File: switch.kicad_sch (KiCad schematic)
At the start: 46 parts, among them Q1 2N7002, U1 RTL8367RB, Y1 25MHz

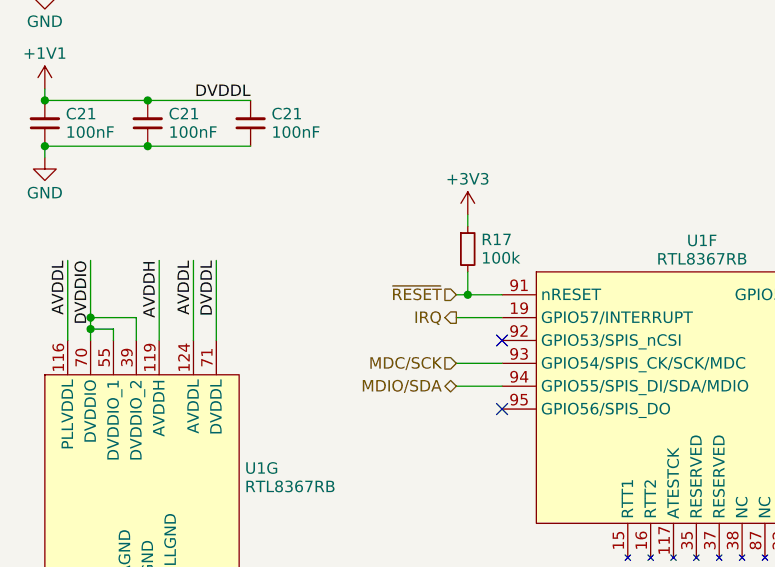
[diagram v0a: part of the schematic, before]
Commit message: Finalize design
- Layout last signals
- Hide designators
- Add more LEDs
- Add tooling holes
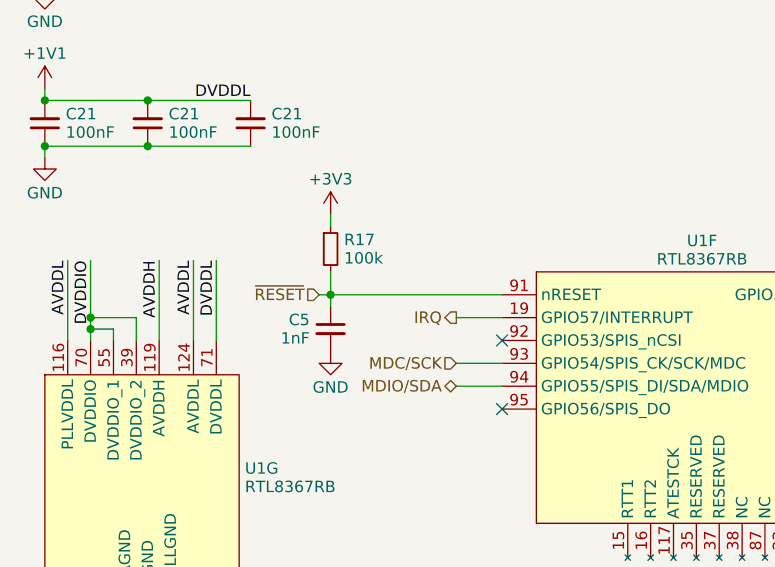
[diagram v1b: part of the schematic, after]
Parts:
- added C5: 1nF, Capacitor_SMD:C_0402_1005Metric, symbol Device:C_Small
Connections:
- net GND: now also C5.2
- net ~{RESET}: now also C5.1
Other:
- moved on the sheet: R17
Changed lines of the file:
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@@
   (junction (at 39.37 77.47) (diameter 0) (color 0 0 0 0)
   )
-  (junction (at 63.5 138.43) (diameter 0) (color 0 0 0 0)
+  (junction (at 48.26 138.43) (diameter 0) (color 0 0 0 0)
   )
   (junction (at 21.59 140.97) (diameter 0) (color 0 0 0 0)
@@
     (stroke (width 0) (type default))
   )
-  (wire (pts (xy 63.5 138.43) (xy 67.31 138.43))
+  (wire (pts (xy 48.26 138.43) (xy 67.31 138.43))
     (stroke (width 0) (type default))
   )
@@
     (stroke (width 0) (type default))
   )
-  (wire (pts (xy 63.5 129.54) (xy 63.5 130.81))
+  (wire (pts (xy 48.26 129.54) (xy 48.26 130.81))
     (stroke (width 0) (type default))
   )
@@
     (stroke (width 0) (type default))
   )
-  (wire (pts (xy 62.23 138.43) (xy 63.5 138.43))
+  (wire (pts (xy 46.99 138.43) (xy 48.26 138.43))
+    (stroke (width 0) (type default))
+  )
+  (wire (pts (xy 48.26 138.43) (xy 48.26 139.7))
     (stroke (width 0) (type default))
   )
@@
     (stroke (width 0) (type default))
   )
-  (wire (pts (xy 63.5 135.89) (xy 63.5 138.43))
+  (wire (pts (xy 48.26 135.89) (xy 48.26 138.43))
     (stroke (width 0) (type default))
   )
@@
     (effects (font (size 1.27 1.27)) (justify left))
   )
-  (hierarchical_label "~{RESET}" (shape input) (at 62.23 138.43 180) (fields_autoplaced)
+  (hierarchical_label "~{RESET}" (shape input) (at 46.99 138.43 180) (fields_autoplaced)
     (effects (font (size 1.27 1.27)) (justify right))
   )
@@
     )
   )
-  (symbol (lib_id "Device:R_Small") (at 63.5 133.35 0) (unit 1)
-    (in_bom yes) (on_board yes) (dnp no) (fields_autoplaced)
-    (property "Reference" "R17" (at 64.9986 132.326 0)
+  (symbol (lib_id "Device:R_Small") (at 48.26 133.35 0) (unit 1)
+    (in_bom yes) (on_board yes) (dnp no) (fields_autoplaced)
+    (property "Reference" "R17" (at 49.7586 132.326 0)
       (effects (font (size 1.27 1.27)) (justify left))
     )
-    (property "Value" "100k" (at 64.9986 134.374 0)
+    (property "Value" "100k" (at 49.7586 134.374 0)
       (effects (font (size 1.27 1.27)) (justify left))
     )
-    (property "Footprint" "Resistor_SMD:R_0402_1005Metric" (at 63.5 133.35 0)
-      (effects (font (size 1.27 1.27)) hide)
-    )
-    (property "Datasheet" "~" (at 63.5 133.35 0)
-      (effects (font (size 1.27 1.27)) hide)
-    )
-    (property "LCSC" "C25741" (at 63.5 133.35 0)
+    (property "Footprint" "Resistor_SMD:R_0402_1005Metric" (at 48.26 133.35 0)
+      (effects (font (size 1.27 1.27)) hide)
+    )
+    (property "Datasheet" "~" (at 48.26 133.35 0)
+      (effects (font (size 1.27 1.27)) hide)
+    )
+    (property "LCSC" "C25741" (at 48.26 133.35 0)
       (effects (font (size 1.27 1.27)) hide)
     )
@@
         (path "/1d58c53f-167c-46c6-b61a-0c5d76c66e31/71e1ec36-fcc5-4ea9-a9bb-92fd21a85ab0"
           (reference "R79") (unit 1)
+        )
+      )
+    )
+  )
+  (symbol (lib_id "Device:C_Small") (at 48.26 142.24 0) (mirror y) (unit 1)
+    (in_bom yes) (on_board yes) (dnp no)
+    (property "Reference" "C5" (at 45.9359 141.2223 0)
+      (effects (font (size 1.27 1.27)) (justify left))
+    )
+    (property "Value" "1nF" (at 45.9359 143.2703 0)
+      (effects (font (size 1.27 1.27)) (justify left))
+    )
+    (property "Footprint" "Capacitor_SMD:C_0402_1005Metric" (at 48.26 142.24 0)
+      (effects (font (size 1.27 1.27)) hide)
+    )
+    (property "Datasheet" "~" (at 48.26 142.24 0)
+      (effects (font (size 1.27 1.27)) hide)
+    )
+    (property "LCSC" "C1523" (at 48.26 142.24 0)
+      (effects (font (size 1.27 1.27)) hide)
+    )
+    (pin "1")
+    (pin "2")
+    (instances
+      (project "OpenHomeSwitch"
+        (path "/1d58c53f-167c-46c6-b61a-0c5d76c66e31/71e1ec36-fcc5-4ea9-a9bb-92fd21a85ab0/fcbac710-5c4c-4f73-a659-520d2a4da378"
+          (reference "C5") (unit 1)
+        )
+        (path "/1d58c53f-167c-46c6-b61a-0c5d76c66e31/71e1ec36-fcc5-4ea9-a9bb-92fd21a85ab0"
+          (reference "C130") (unit 1)
         )
       )
@@
     )
   )
+  (symbol (lib_id "power:GND") (at 48.26 144.78 0) (unit 1)
+    (in_bom yes) (on_board yes) (dnp no) (fields_autoplaced)
+    (property "Reference" "#PWR0141" (at 48.26 151.13 0)
+      (effects (font (size 1.27 1.27)) hide)
+    )
+    (property "Value" "GND" (at 48.26 148.725 0)
+      (effects (font (size 1.27 1.27)))
+    )
+    (property "Footprint" "" (at 48.26 144.78 0)
+      (effects (font (size 1.27 1.27)) hide)
+    )
+    (property "Datasheet" "" (at 48.26 144.78 0)
+      (effects (font (size 1.27 1.27)) hide)
+    )
+    (pin "1")
+    (instances
+      (project "OpenHomeSwitch"
+        (path "/1d58c53f-167c-46c6-b61a-0c5d76c66e31/71e1ec36-fcc5-4ea9-a9bb-92fd21a85ab0"
+          (reference "#PWR0141") (unit 1)
+        )
+      )
+    )
+  )
   (symbol (lib_id "Device:C_Small") (at 201.93 113.03 90) (mirror x) (unit 1)
     (in_bom yes) (on_board yes) (dnp no)
@@
     )
   )
-  (symbol (lib_id "power:+3V3") (at 63.5 129.54 0) (unit 1)
-    (in_bom yes) (on_board yes) (dnp no) (fields_autoplaced)
-    (property "Reference" "#PWR0128" (at 63.5 133.35 0)
-      (effects (font (size 1.27 1.27)) hide)
-    )
-    (property "Value" "+3V3" (at 63.5 125.595 0)
-      (effects (font (size 1.27 1.27)))
-    )
-    (property "Footprint" "" (at 63.5 129.54 0)
-      (effects (font (size 1.27 1.27)) hide)
-    )
-    (property "Datasheet" "" (at 63.5 129.54 0)
-      (effects (font (size 1.27 1.27)) hide)
-    )
+  (symbol (lib_id "power:+3V3") (at 48.26 129.54 0) (unit 1)
+    (in_bom yes) (on_board yes) (dnp no) (fields_autoplaced)
+    (property "Reference" "#PWR0128" (at 48.26 133.35 0)
+      (effects (font (size 1.27 1.27)) hide)
+    )
+    (property "Value" "+3V3" (at 48.26 125.595 0)
+      (effects (font (size 1.27 1.27)))
+    )
+    (property "Footprint" "" (at 48.26 129.54 0)
+      (effects (font (size 1.27 1.27)) hide)
+    )
+    (property "Datasheet" "" (at 48.26 129.54 0)
+      (effects (font (size 1.27 1.27)) hide)
+    )

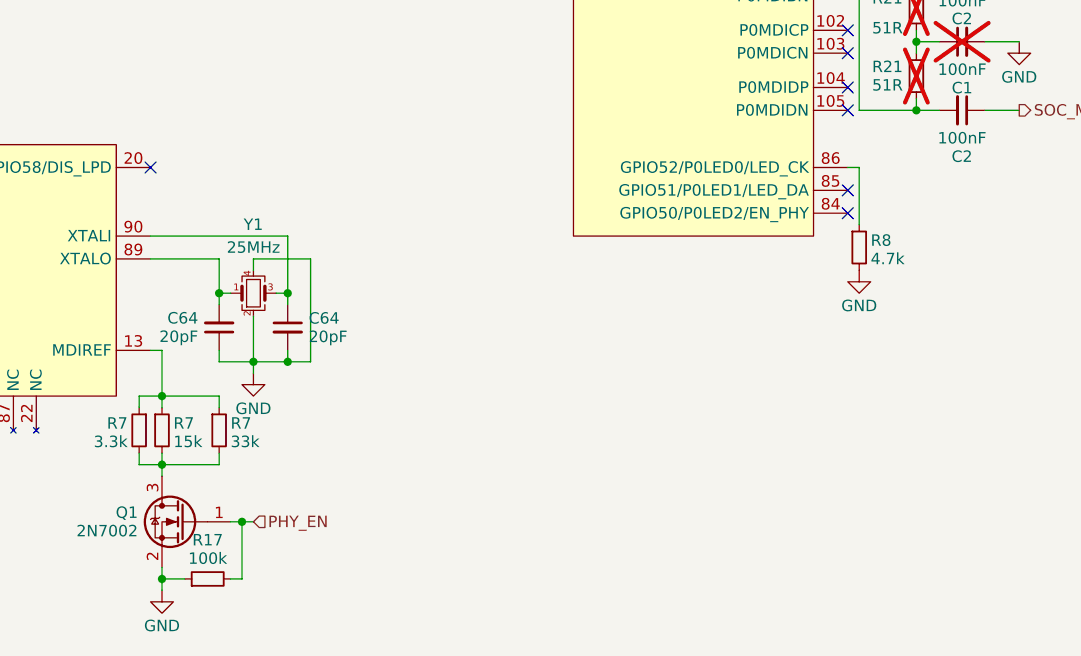
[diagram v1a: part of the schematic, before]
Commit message: Change switch control to I2C
MDIO has proven too slow, use I2C instead
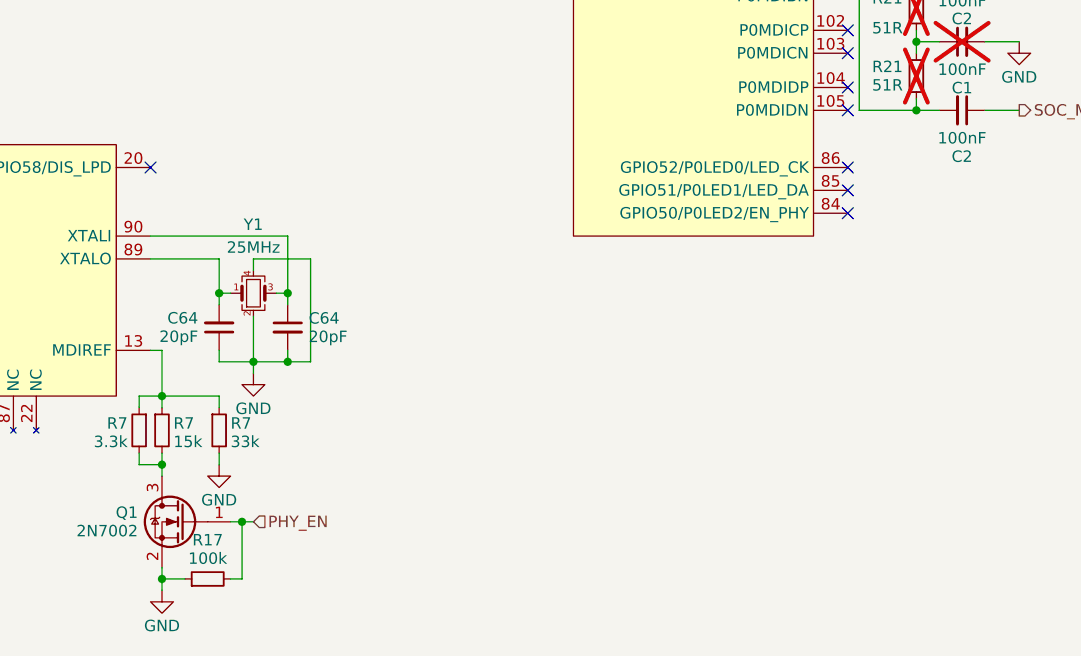
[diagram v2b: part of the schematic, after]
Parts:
- removed R8: 4.7k, Resistor_SMD:R_0402_1005Metric, symbol Device:R_Small
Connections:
- net GND: now also R7.2
- net at Q1.3 (D), R7.2, R7.2: no longer R7.2
- no-connect marks 9 -> 10
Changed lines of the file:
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@@
   (no_connect (at 67.31 151.13))
   (no_connect (at 189.23 123.19))
+  (no_connect (at 189.23 138.43))
   (no_connect (at 189.23 125.73))
   (no_connect (at 189.23 143.51))
@@
     (stroke (width 0) (type default))
   )
-  (wire (pts (xy 190.5 138.43) (xy 189.23 138.43))
-    (stroke (width 0) (type default))
-  )
   (wire (pts (xy 16.51 97.79) (xy 22.86 97.79))
     (stroke (width 0) (type default))
@@
     (stroke (width 0) (type default))
   )
-  (wire (pts (xy 190.5 144.78) (xy 190.5 138.43))
-    (stroke (width 0) (type default))
-  )
   (wire (pts (xy 190.5 97.79) (xy 196.85 97.79))
     (stroke (width 0) (type default))
@@
   )
   (wire (pts (xy 156.21 76.2) (xy 158.75 76.2))
-    (stroke (width 0) (type default))
-  )
-  (wire (pts (xy 113.03 171.45) (xy 119.38 171.45))
     (stroke (width 0) (type default))
   )
@@
     )
   )
-  (symbol (lib_id "power:GND") (at 190.5 149.86 0) (unit 1)
-    (in_bom yes) (on_board yes) (dnp no) (fields_autoplaced)
-    (property "Reference" "#PWR061" (at 190.5 156.21 0)
-      (effects (font (size 1.27 1.27)) hide)
-    )
-    (property "Value" "GND" (at 190.5 153.805 0)
-      (effects (font (size 1.27 1.27)))
-    )
-    (property "Footprint" "" (at 190.5 149.86 0)
-      (effects (font (size 1.27 1.27)) hide)
-    )
-    (property "Datasheet" "" (at 190.5 149.86 0)
-      (effects (font (size 1.27 1.27)) hide)
-    )
-    (pin "1")
-    (instances
-      (project "OpenHomeSwitch"
-        (path "/1d58c53f-167c-46c6-b61a-0c5d76c66e31/71e1ec36-fcc5-4ea9-a9bb-92fd21a85ab0"
-          (reference "#PWR061") (unit 1)
-        )
-      )
-    )
-  )
   (symbol (lib_id "Device:C_Small") (at 201.93 116.84 90) (unit 1)
     (in_bom yes) (on_board yes) (dnp no)
@@
     )
   )
+  (symbol (lib_id "power:GND") (at 119.38 171.45 0) (unit 1)
+    (in_bom yes) (on_board yes) (dnp no) (fields_autoplaced)
+    (property "Reference" "#PWR0170" (at 119.38 177.8 0)
+      (effects (font (size 1.27 1.27)) hide)
+    )
+    (property "Value" "GND" (at 119.38 175.395 0)
+      (effects (font (size 1.27 1.27)))
+    )
+    (property "Footprint" "" (at 119.38 171.45 0)
+      (effects (font (size 1.27 1.27)) hide)
+    )
+    (property "Datasheet" "" (at 119.38 171.45 0)
+      (effects (font (size 1.27 1.27)) hide)
+    )
+    (pin "1")
+    (instances
+      (project "OpenHomeSwitch"
+        (path "/1d58c53f-167c-46c6-b61a-0c5d76c66e31/71e1ec36-fcc5-4ea9-a9bb-92fd21a85ab0"
+          (reference "#PWR0170") (unit 1)
+        )
+      )
+    )
+  )
   (symbol (lib_id "Ethernet_Switch_Realtek:RTL8367RB-VB") (at 90.17 153.67 0) (unit 6)
     (in_bom yes) (on_board yes) (dnp no) (fields_autoplaced)
@@
         )
       )
-    )
-  )
-  (symbol (lib_id "Device:R_Small") (at 190.5 147.32 0) (unit 1)
-    (in_bom yes) (on_board yes) (dnp no)
-    (property "Reference" "R8" (at 191.77 146.542 0)
-      (effects (font (size 1.27 1.27)) (justify left))
-    )
-    (property "Value" "4.7k" (at 191.77 148.59 0)
-      (effects (font (size 1.27 1.27)) (justify left))
-    )
-    (property "Footprint" "Resistor_SMD:R_0402_1005Metric" (at 190.5 147.32 0)
-      (effects (font (size 1.27 1.27)) hide)
-    )
-    (property "Datasheet" "" (at 190.5 147.32 0)
-      (effects (font (size 1.27 1.27)) hide)
-    )
-    (property "LCSC" "C25900" (at 190.5 147.32 0)
-      (effects (font (size 1.27 1.27)) hide)
-    )
-    (pin "1")
-    (pin "2")
-    (instances
-      (project "OpenHomeSwitch"
-        (path "/1d58c53f-167c-46c6-b61a-0c5d76c66e31/71e1ec36-fcc5-4ea9-a9bb-92fd21a85ab0/fcbac710-5c4c-4f73-a659-520d2a4da378"
-          (reference "R8") (unit 1)
-        )
-        (path "/1d58c53f-167c-46c6-b61a-0c5d76c66e31/71e1ec36-fcc5-4ea9-a9bb-92fd21a85ab0"
-          (reference "R43") (unit 1)
-        )
-      )
